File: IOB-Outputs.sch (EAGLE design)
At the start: 27 parts, among them CON1 CONNECTOR-IO4STD, Q1 MOSFET-N, Q10 MOSFET-P, Q11 MOSFET-P, Q12 MOSFET-P, Q2 MOSFET-N, Q3 MOSFET-N, Q4 MOSFET-N, Q5 MOSFET-N, Q6 MOSFET-N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

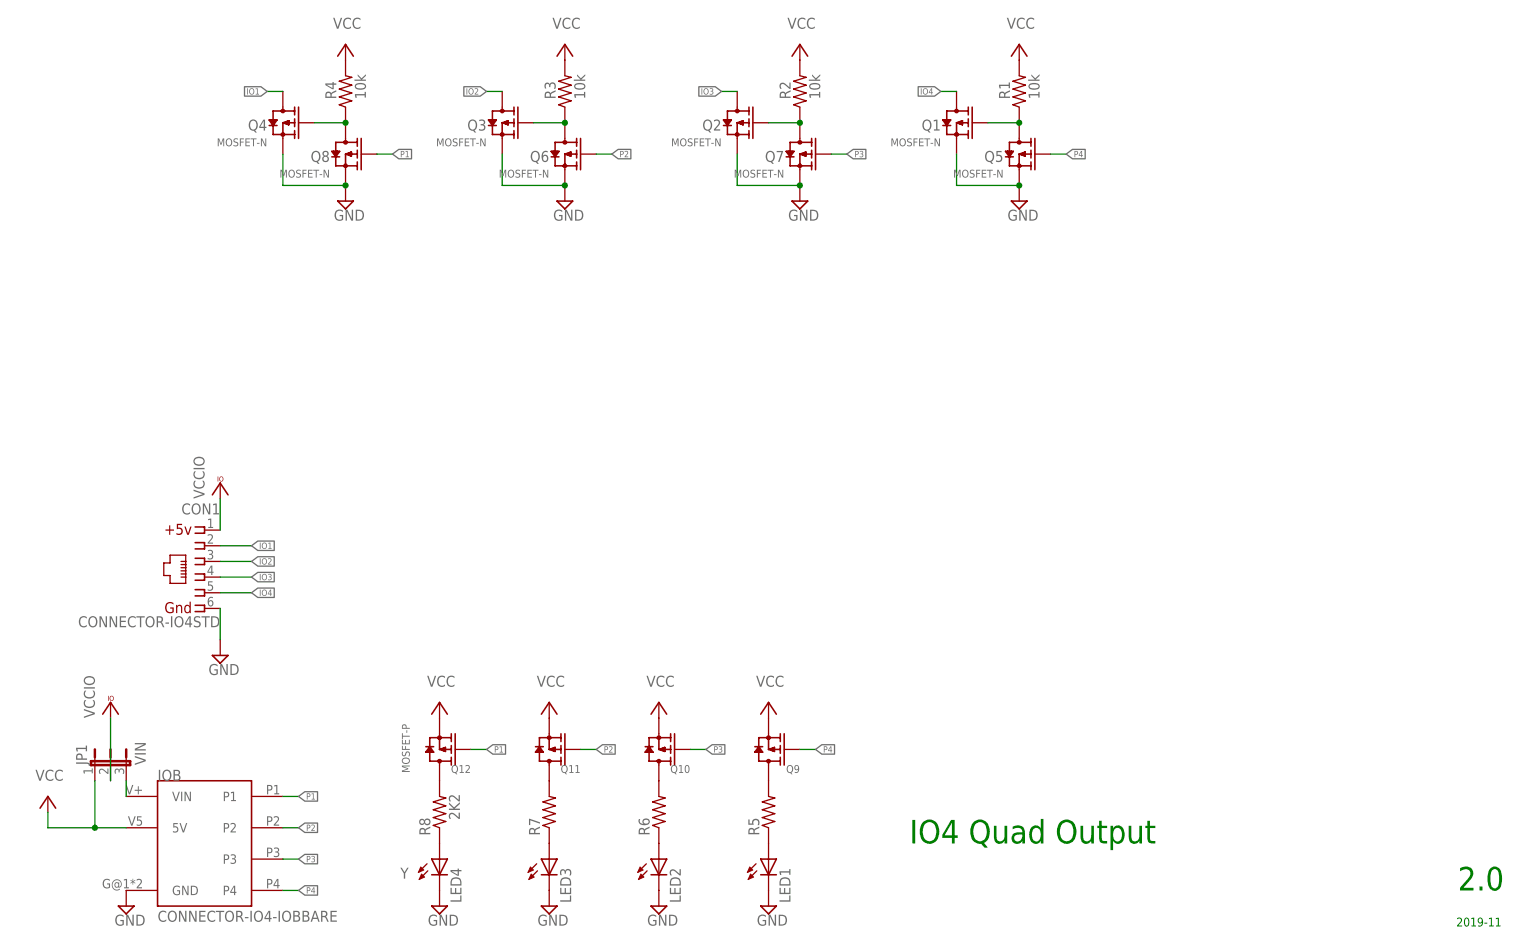
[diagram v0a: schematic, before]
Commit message: updated to new IOB design
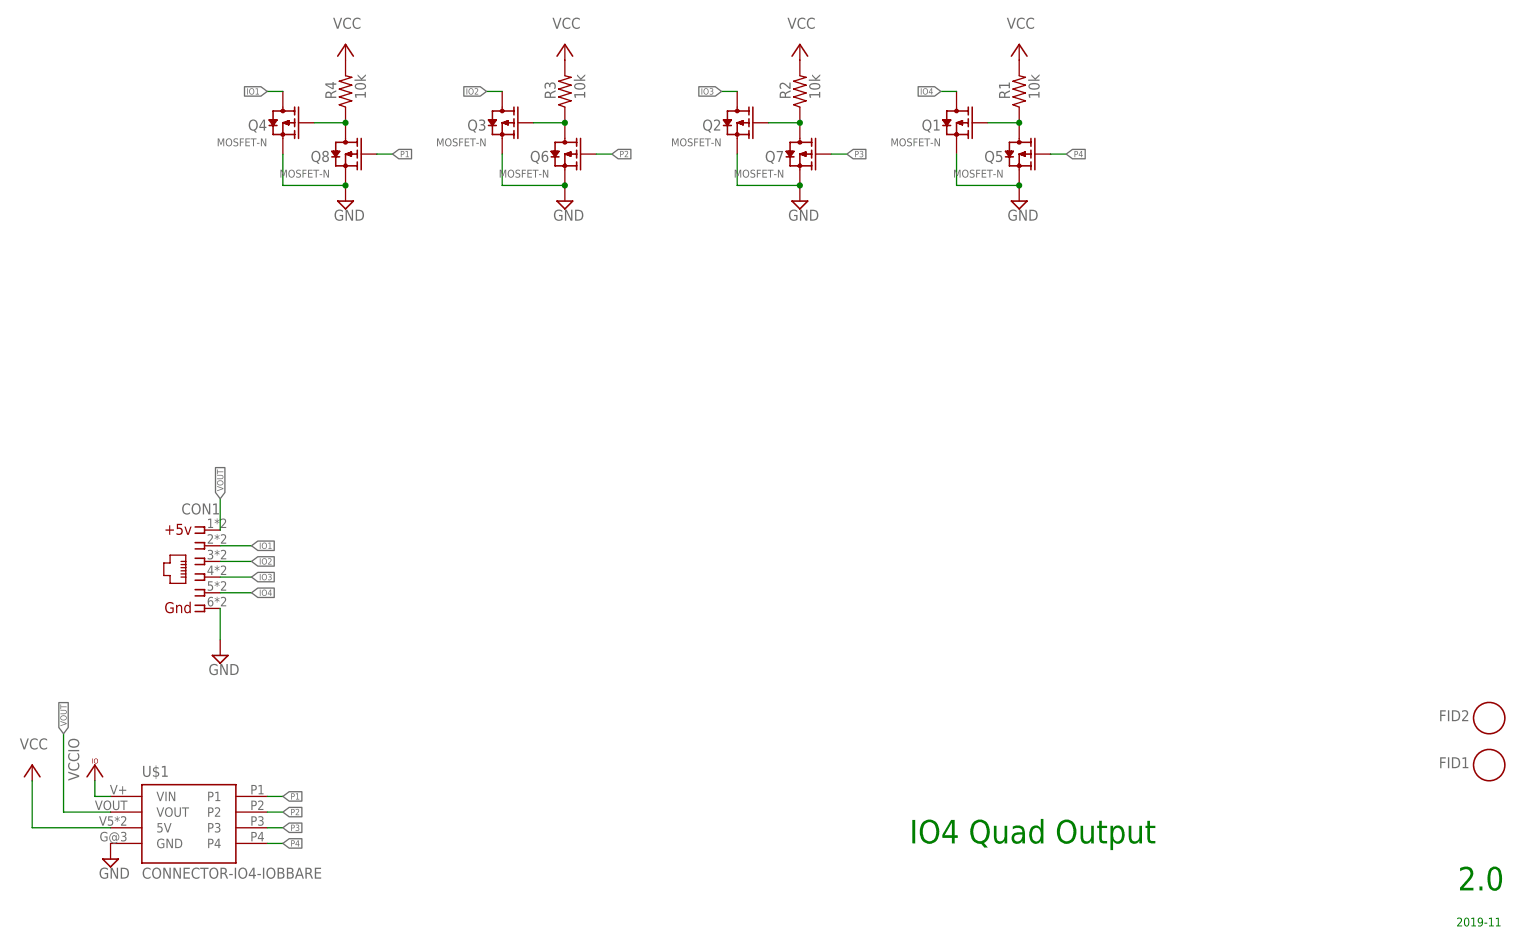
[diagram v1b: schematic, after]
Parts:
- removed IOB: CONNECTOR-IO4-IOBBARE, SPCoast:CONNECTOR-IO4-IOBBARE
- removed JP1: VIN, SPCoast:JUMPER-3PTH-LOCK
- removed LED1, LED2, LED3, LED4: Y, SPCoast:LED0603-LED
- removed Q10, Q11, Q12, Q9: MOSFET-P, SPCoast:MOSFET-P
- removed R5, R6, R7, R8: 2K2, SPCoast:R0805-RES
- added FID1, FID2: FIDUCIAL, SPCoast:FIDUCIAL
- added U$1: CONNECTOR-IO4-IOBBARE, SPCoast:CONNECTOR-IO4-IOBBARE
- CON1: value CONNECTOR-IO4STD -> (none); device SPCoast:CONNECTOR-IO4STD -> SPCoast:CONNECTOR-IO4IPINS
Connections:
- removed net N$11: Q12.D, R8.2
- removed net N$2: LED4.A, R8.1
- removed net N$3: LED3.A, R7.1
- removed net N$30: Q11.D, R7.2
- removed net N$31: Q10.D, R6.2
- removed net N$32: Q9.D, R5.2
- removed net N$4: LED2.A, R6.1
- removed net N$5: LED1.A, R5.1
- removed net VCCIO: CON1.1, JP1.2
- new net VOUT: CON1.1, U$1.VOUT
- net GND: now also U$1.GND; no longer IOB.GND, LED1.C, LED2.C, LED3.C, LED4.C
- net P1: now also U$1.P1; no longer IOB.P1, Q12.G
- net P2: now also U$1.P2; no longer IOB.P2, Q11.G
- net P3: now also U$1.P3; no longer IOB.P3, Q10.G
- net P4: now also U$1.P4; no longer IOB.P4, Q9.G
- net VCC: now also U$1.5V; no longer IOB.5V, JP1.1, Q10.S, Q11.S, Q12.S, Q9.S
- net VIN: now also U$1.VIN; no longer IOB.VIN, JP1.3
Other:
- moved on the sheet: CON1

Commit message: bump version
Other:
- note added: "2020.03"
- note added: "3.0"
- note added: "Changes: New IOB design"
- note removed: "2.0"
- note removed: "2019-11"
- note removed: "Changes: Output only - non-inverting Open Drain current sink"
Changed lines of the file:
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@@
 <plain>
 <text x="149.86" y="20.32" size="3.81" layer="91">IO4 Quad Output</text>
-<text x="238.76" y="12.7" size="3.81" layer="91">2.0</text>
-<text x="238.506" y="6.858" size="1.4224" layer="91">2019-11</text>
-<text x="7.62" y="180.34" size="1.27" layer="102">Changes: Output only - non-inverting Open Drain current sink</text>
+<text x="238.76" y="12.7" size="3.81" layer="91">3.0</text>
+<text x="238.506" y="6.858" size="1.4224" layer="91">2020.03</text>
+<text x="7.62" y="180.34" size="1.27" layer="102">Changes: New IOB design</text>
 </plain>
 <instances>

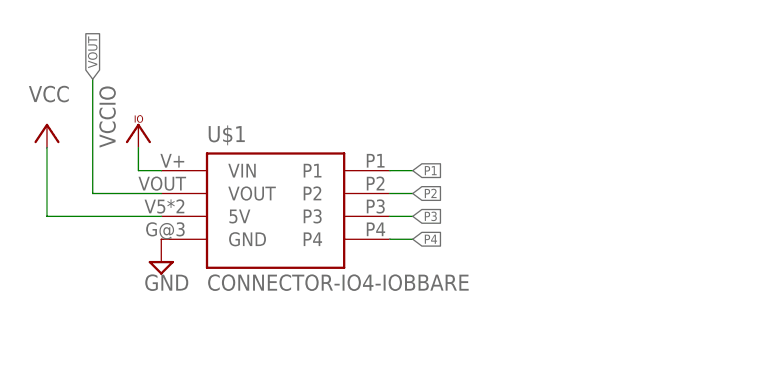
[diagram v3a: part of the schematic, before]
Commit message: normalized silkscreen layout across IOBs
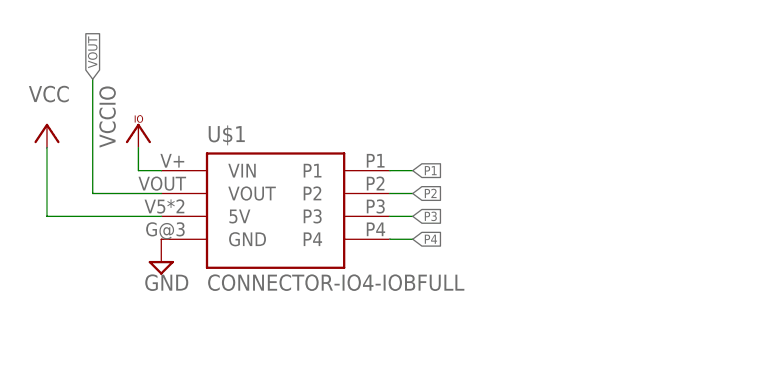
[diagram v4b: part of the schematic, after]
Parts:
- U$1: value CONNECTOR-IO4-IOBBARE -> CONNECTOR-IO4-IOBFULL; device SPCoast:CONNECTOR-IO4-IOBBARE -> SPCoast:CONNECTOR-IO4-IOBFULL
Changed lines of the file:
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@@
 <part name="P+9" library="supply1" deviceset="VCC" device=""/>
 <part name="CON1" library="SPCoast" deviceset="CONNECTOR-IO4" device="IPINS"/>
-<part name="U$1" library="SPCoast" deviceset="CONNECTOR-IO4-IOB" device="BARE"/>
+<part name="U$1" library="SPCoast" deviceset="CONNECTOR-IO4-IOB" device="FULL"/>
 <part name="P+1" library="supply1" deviceset="VCC" device=""/>
 <part name="VCC1" library="SPCoast" deviceset="VCCIO" device=""/>
